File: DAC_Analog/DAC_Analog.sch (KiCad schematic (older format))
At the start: 17 parts, among them J1 SPDIF_RX_1, J2 SPDIF_RX_2, J3 SPDIF_RX_3, J4 SPDIF_RX_4, J5 I2C_IN, J6 OutR, J7 OutL, J8 Alim_DAC, J9 Alim_SRC, U1 ISO154x

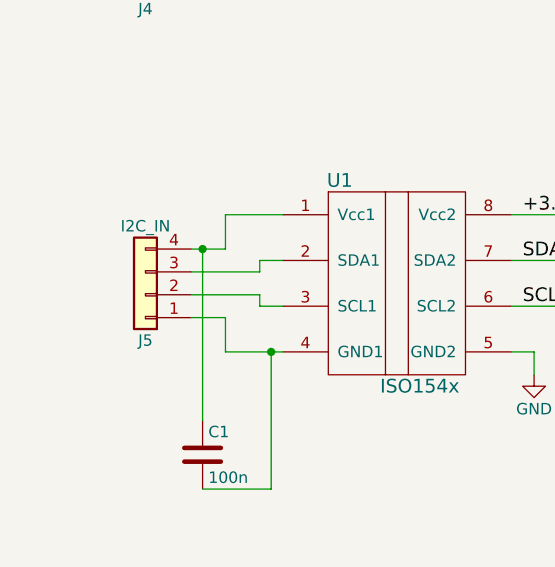
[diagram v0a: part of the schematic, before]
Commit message: Place cmp DAC_Analog
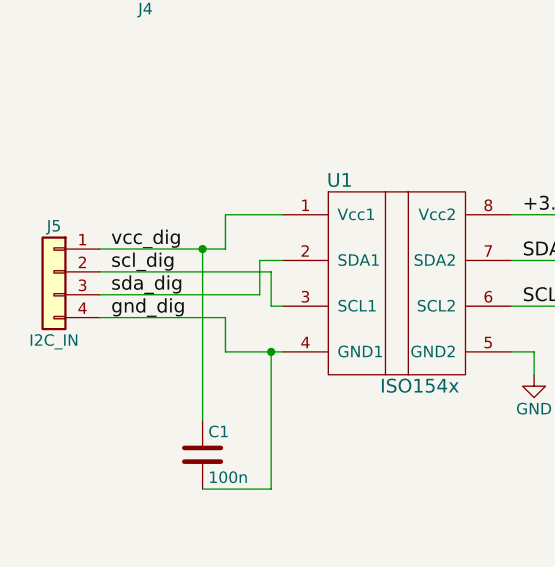
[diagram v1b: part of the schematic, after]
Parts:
- C3, C4, C5, C6, C7: footprint Capacitors_THT:CP_Radial_Tantal_D8.0mm_P2.50mm -> Capacitors_Tantalum_SMD:CP_Tantalum_Case-C_EIA-6032-28_Hand
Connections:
- net labels added: gnd_dig, scl_dig, sda_dig, vcc_dig
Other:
- moved on the sheet: J5
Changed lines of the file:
@@
 L Conn_01x04 J5
 U 1 1 59C97424
-P 1300 3800
-F 0 "J5" H 1300 4000 50  0000 C CNN
-F 1 "I2C_IN" H 1300 3500 50  0000 C CNN
-F 2 "Pin_Headers:Pin_Header_Straight_1x04_Pitch2.54mm" H 1300 3800 50  0001 C CNN
-F 3 "" H 1300 3800 50  0001 C CNN
-	1    1300 3800
-	-1   0    0    1
+P 900 3700
+F 0 "J5" H 900 3900 50  0000 C CNN
+F 1 "I2C_IN" H 900 3400 50  0000 C CNN
+F 2 "Pin_Headers:Pin_Header_Straight_1x04_Pitch2.54mm" H 900 3700 50  0001 C CNN
+F 3 "" H 900 3700 50  0001 C CNN
+	1    900  3700
+	-1   0    0    -1
 $EndComp
 $Comp
@@
 	2900 3450 3700 3450
 Wire Wire Line
-	1500 3600 1650 3600
+	1100 3600 1650 3600
 Wire Wire Line
 	1650 3600 1650 3450
@@
 	1650 3450 1900 3450
 Wire Wire Line
-	1500 3700 1800 3700
-Wire Wire Line
-	1800 3700 1800 3650
-Wire Wire Line
-	1800 3650 1900 3650
-Wire Wire Line
-	1500 3800 1800 3800
-Wire Wire Line
-	1800 3800 1800 3850
-Wire Wire Line
-	1800 3850 1900 3850
-Wire Wire Line
-	1500 3900 1650 3900
+	1100 3800 1800 3800
+Wire Wire Line
+	1100 3900 1650 3900
 Wire Wire Line
 	1650 3900 1650 4050
@@
 F 0 "C4" H 4475 5550 50  0000 L CNN
 F 1 "100u" H 4475 5350 50  0000 L CNN
-F 2 "Capacitors_THT:CP_Radial_Tantal_D8.0mm_P2.50mm" H 4488 5300 50  0001 C CNN
+F 2 "Capacitors_Tantalum_SMD:CP_Tantalum_Case-C_EIA-6032-28_Hand" H 4488 5300 50  0001 C CNN
 F 3 "" H 4450 5450 50  0001 C CNN
 	1    4450 5450
@@
 F 0 "C6" H 5225 5550 50  0000 L CNN
 F 1 "100u" H 5225 5350 50  0000 L CNN
-F 2 "Capacitors_THT:CP_Radial_Tantal_D8.0mm_P2.50mm" H 5238 5300 50  0001 C CNN
+F 2 "Capacitors_Tantalum_SMD:CP_Tantalum_Case-C_EIA-6032-28_Hand" H 5238 5300 50  0001 C CNN
 F 3 "" H 5200 5450 50  0001 C CNN
 	1    5200 5450
@@
 F 0 "C7" H 5975 5550 50  0000 L CNN
 F 1 "100u" H 5975 5350 50  0000 L CNN
-F 2 "Capacitors_THT:CP_Radial_Tantal_D8.0mm_P2.50mm" H 5988 5300 50  0001 C CNN
+F 2 "Capacitors_Tantalum_SMD:CP_Tantalum_Case-C_EIA-6032-28_Hand" H 5988 5300 50  0001 C CNN
 F 3 "" H 5950 5450 50  0001 C CNN
 	1    5950 5450
@@
 F 0 "C5" H 5175 6400 50  0000 L CNN
 F 1 "100u" H 5175 6200 50  0000 L CNN
-F 2 "Capacitors_THT:CP_Radial_Tantal_D8.0mm_P2.50mm" H 5188 6150 50  0001 C CNN
+F 2 "Capacitors_Tantalum_SMD:CP_Tantalum_Case-C_EIA-6032-28_Hand" H 5188 6150 50  0001 C CNN
 F 3 "" H 5150 6300 50  0001 C CNN
 	1    5150 6300
@@
 F 0 "C3" H 4425 6400 50  0000 L CNN
 F 1 "100u" H 4425 6200 50  0000 L CNN
-F 2 "Capacitors_THT:CP_Radial_Tantal_D8.0mm_P2.50mm" H 4438 6150 50  0001 C CNN
+F 2 "Capacitors_Tantalum_SMD:CP_Tantalum_Case-C_EIA-6032-28_Hand" H 4438 6150 50  0001 C CNN
 F 3 "" H 4400 6300 50  0001 C CNN
 	1    4400 6300
@@
 Wire Wire Line
 	7750 3850 8250 3850
+Text Label 1150 3900 0    60   ~ 0
+gnd_dig
+Text Label 1150 3700 0    60   ~ 0
+scl_dig
+Text Label 1150 3800 0    60   ~ 0
+sda_dig
+Text Label 1150 3600 0    60   ~ 0
+vcc_dig
+Wire Wire Line
+	1100 3700 1850 3700
+Wire Wire Line
+	1850 3700 1850 3850
+Wire Wire Line
+	1850 3850 1900 3850
+Wire Wire Line
+	1800 3800 1800 3650
+Wire Wire Line
+	1800 3650 1900 3650
 $EndSCHEMATC

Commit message: Update layout
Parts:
- added D1, D2, D3, D4, D5: LED, Yame_library:SM0603-LED-MR, symbol LED
- added R31, R32, R33, R34, R35: R, Yame_library:SM0603-MR, symbol R
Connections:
- wire segments 91 -> 106
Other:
- moved on the sheet: C3, C4, C5, C7

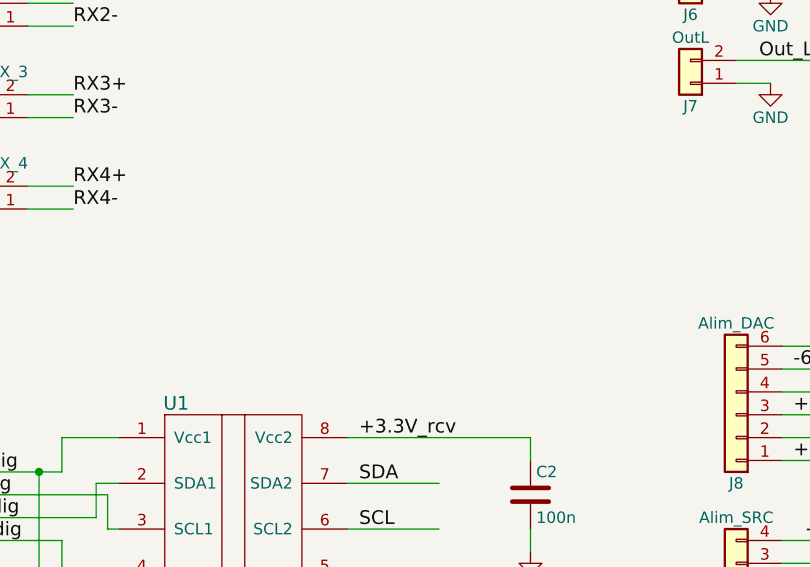
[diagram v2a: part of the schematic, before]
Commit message: DAC_Analog : place all cmp
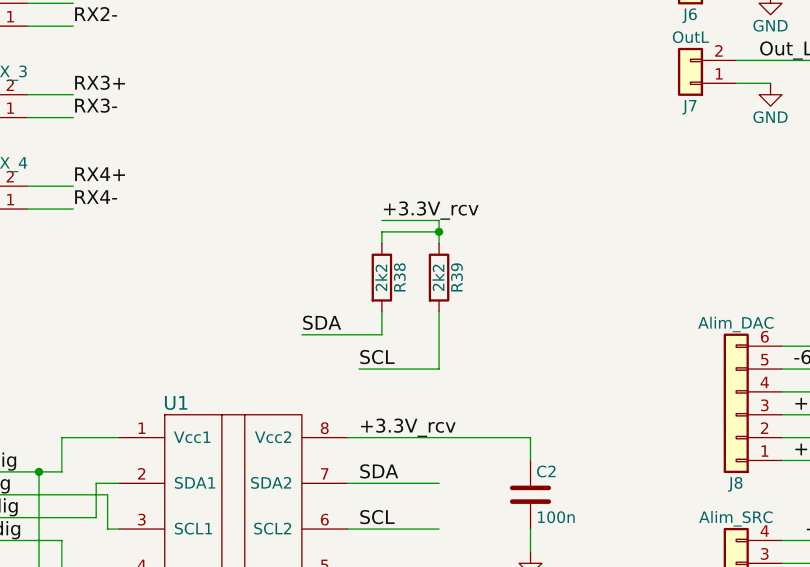
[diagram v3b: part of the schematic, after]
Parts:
- added R38, R39: 2k2, Yame_library:SM0603-MR, symbol R
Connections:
- wire segments 106 -> 114
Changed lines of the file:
@@
 	1650 4050 1900 4050
 $Comp
-L GND #PWR01
+L GND #PWR1
 U 1 1 59CB983A
 P 3000 4150
-F 0 "#PWR01" H 3000 3900 50  0001 C CNN
+F 0 "#PWR1" H 3000 3900 50  0001 C CNN
 F 1 "GND" H 3000 4000 50  0000 C CNN
 F 2 "" H 3000 4150 50  0001 C CNN
@@
 	7850 2250 8250 2250
 $Comp
-L GND #PWR02
+L GND #PWR17
 U 1 1 59CBC1FC
 P 7750 4100
-F 0 "#PWR02" H 7750 3850 50  0001 C CNN
+F 0 "#PWR17" H 7750 3850 50  0001 C CNN
 F 1 "GND" H 7750 3950 50  0000 C CNN
 F 2 "" H 7750 4100 50  0001 C CNN
@@
 	7750 4000 7750 4100
 $Comp
-L GND #PWR03
+L GND #PWR16
 U 1 1 59CBC549
 P 7500 1450
-F 0 "#PWR03" H 7500 1200 50  0001 C CNN
+F 0 "#PWR16" H 7500 1200 50  0001 C CNN
 F 1 "GND" H 7500 1300 50  0000 C CNN
 F 2 "" H 7500 1450 50  0001 C CNN
@@
 	4600 1800 5000 1800
 $Comp
-L GND #PWR04
+L GND #PWR7
 U 1 1 59CBD970
 P 4750 1500
-F 0 "#PWR04" H 4750 1250 50  0001 C CNN
+F 0 "#PWR7" H 4750 1250 50  0001 C CNN
 F 1 "GND" H 4750 1350 50  0000 C CNN
 F 2 "" H 4750 1500 50  0001 C CNN
@@
 $EndComp
 $Comp
-L GND #PWR05
+L GND #PWR8
 U 1 1 59CBD9E8
 P 4750 1900
-F 0 "#PWR05" H 4750 1650 50  0001 C CNN
+F 0 "#PWR8" H 4750 1650 50  0001 C CNN
 F 1 "GND" H 4750 1750 50  0000 C CNN
 F 2 "" H 4750 1900 50  0001 C CNN
@@
 	3700 3450 3700 3550
 $Comp
-L GND #PWR06
+L GND #PWR2
 U 1 1 59CC829B
 P 3700 3950
-F 0 "#PWR06" H 3700 3700 50  0001 C CNN
+F 0 "#PWR2" H 3700 3700 50  0001 C CNN
 F 1 "GND" H 3700 3800 50  0000 C CNN
 F 2 "" H 3700 3950 50  0001 C CNN
@@
 $EndComp
 $Comp
-L GND #PWR07
+L GND #PWR12
 U 1 1 59CC3026
 P 5450 4300
-F 0 "#PWR07" H 5450 4050 50  0001 C CNN
+F 0 "#PWR12" H 5450 4050 50  0001 C CNN
 F 1 "GND" H 5450 4150 50  0000 C CNN
 F 2 "" H 5450 4300 50  0001 C CNN
@@
 $EndComp
 $Comp
-L GND #PWR08
+L GND #PWR4
 U 1 1 59CCA544
 P 4350 5700
-F 0 "#PWR08" H 4350 5450 50  0001 C CNN
+F 0 "#PWR4" H 4350 5450 50  0001 C CNN
 F 1 "GND" H 4350 5550 50  0000 C CNN
 F 2 "" H 4350 5700 50  0001 C CNN
@@
 $EndComp
 $Comp
-L GND #PWR09
+L GND #PWR10
 U 1 1 59CCA62A
 P 5200 5700
-F 0 "#PWR09" H 5200 5450 50  0001 C CNN
+F 0 "#PWR10" H 5200 5450 50  0001 C CNN
 F 1 "GND" H 5200 5550 50  0000 C CNN
 F 2 "" H 5200 5700 50  0001 C CNN
@@
 $EndComp
 $Comp
-L GND #PWR010
+L GND #PWR15
 U 1 1 59CCA710
 P 6050 5700
-F 0 "#PWR010" H 6050 5450 50  0001 C CNN
+F 0 "#PWR15" H 6050 5450 50  0001 C CNN
 F 1 "GND" H 6050 5550 50  0000 C CNN
 F 2 "" H 6050 5700 50  0001 C CNN
@@
 $EndComp
 $Comp
-L GND #PWR011
+L GND #PWR14
 U 1 1 59CCA7F6
 P 5700 6950
-F 0 "#PWR011" H 5700 6700 50  0001 C CNN
+F 0 "#PWR14" H 5700 6700 50  0001 C CNN
 F 1 "GND" H 5700 6800 50  0000 C CNN
 F 2 "" H 5700 6950 50  0001 C CNN
@@
 $EndComp
 $Comp
-L GND #PWR012
+L GND #PWR9
 U 1 1 59CCA8DC
 P 4950 6950
-F 0 "#PWR012" H 4950 6700 50  0001 C CNN
+F 0 "#PWR9" H 4950 6700 50  0001 C CNN
 F 1 "GND" H 4950 6800 50  0000 C CNN
 F 2 "" H 4950 6950 50  0001 C CNN
@@
 $EndComp
 $Comp
-L GND #PWR013
+L GND #PWR13
 U 1 1 59EF6504
 P 5550 6000
-F 0 "#PWR013" H 5550 5750 50  0001 C CNN
+F 0 "#PWR13" H 5550 5750 50  0001 C CNN
 F 1 "GND" H 5550 5850 50  0000 C CNN
 F 2 "" H 5550 6000 50  0001 C CNN
@@
 $EndComp
 $Comp
-L GND #PWR014
+L GND #PWR3
 U 1 1 59EF74CB
 P 3850 6000
-F 0 "#PWR014" H 3850 5750 50  0001 C CNN
+F 0 "#PWR3" H 3850 5750 50  0001 C CNN
 F 1 "GND" H 3850 5850 50  0000 C CNN
 F 2 "" H 3850 6000 50  0001 C CNN
@@
 $EndComp
 $Comp
-L GND #PWR015
+L GND #PWR6
 U 1 1 59EF75DC
 P 4700 6000
-F 0 "#PWR015" H 4700 5750 50  0001 C CNN
+F 0 "#PWR6" H 4700 5750 50  0001 C CNN
 F 1 "GND" H 4700 5850 50  0000 C CNN
 F 2 "" H 4700 6000 50  0001 C CNN
@@
 $EndComp
 $Comp
-L GND #PWR016
+L GND #PWR5
 U 1 1 59EF7B17
 P 4500 7250
-F 0 "#PWR016" H 4500 7000 50  0001 C CNN
+F 0 "#PWR5" H 4500 7000 50  0001 C CNN
 F 1 "GND" H 4500 7100 50  0000 C CNN
 F 2 "" H 4500 7250 50  0001 C CNN
@@
 $EndComp
 $Comp
-L GND #PWR017
+L GND #PWR11
 U 1 1 59EF7C3C
 P 5250 7250
-F 0 "#PWR017" H 5250 7000 50  0001 C CNN
+F 0 "#PWR11" H 5250 7000 50  0001 C CNN
 F 1 "GND" H 5250 7100 50  0000 C CNN
 F 2 "" H 5250 7250 50  0001 C CNN
@@
 Wire Wire Line
 	5250 6550 5250 6450
+$Comp
+L R R38
+U 1 1 59EFD621
+P 3050 2750
+F 0 "R38" V 3130 2750 50  0000 C CNN
+F 1 "2k2" V 3050 2750 50  0000 C CNN
+F 2 "Yame_library:SM0603-MR" V 2980 2750 50  0001 C CNN
+F 3 "" H 3050 2750 50  0001 C CNN
+	1    3050 2750
+	1    0    0    -1
+$EndComp
+$Comp
+L R R39
+U 1 1 59EFDBA2
+P 3300 2750
+F 0 "R39" V 3380 2750 50  0000 C CNN
+F 1 "2k2" V 3300 2750 50  0000 C CNN
+F 2 "Yame_library:SM0603-MR" V 3230 2750 50  0001 C CNN
+F 3 "" H 3300 2750 50  0001 C CNN
+	1    3300 2750
+	1    0    0    -1
+$EndComp
+Text Label 3050 2500 0    60   ~ 0
++3.3V_rcv
+Wire Wire Line
+	3050 2500 3300 2500
+Wire Wire Line
+	3300 2500 3300 2600
+Wire Wire Line
+	3050 2600 3050 2550
+Wire Wire Line
+	3050 2550 3300 2550
+Connection ~ 3300 2550
+Text Label 2950 3150 0    60   ~ 0
+SCL
+Text Label 2700 3000 0    60   ~ 0
+SDA
+Wire Wire Line
+	2950 3150 3300 3150
+Wire Wire Line
+	3050 3000 2700 3000
+Wire Wire Line
+	3050 3000 3050 2900
+Wire Wire Line
+	3300 3150 3300 2900
 $EndSCHEMATC

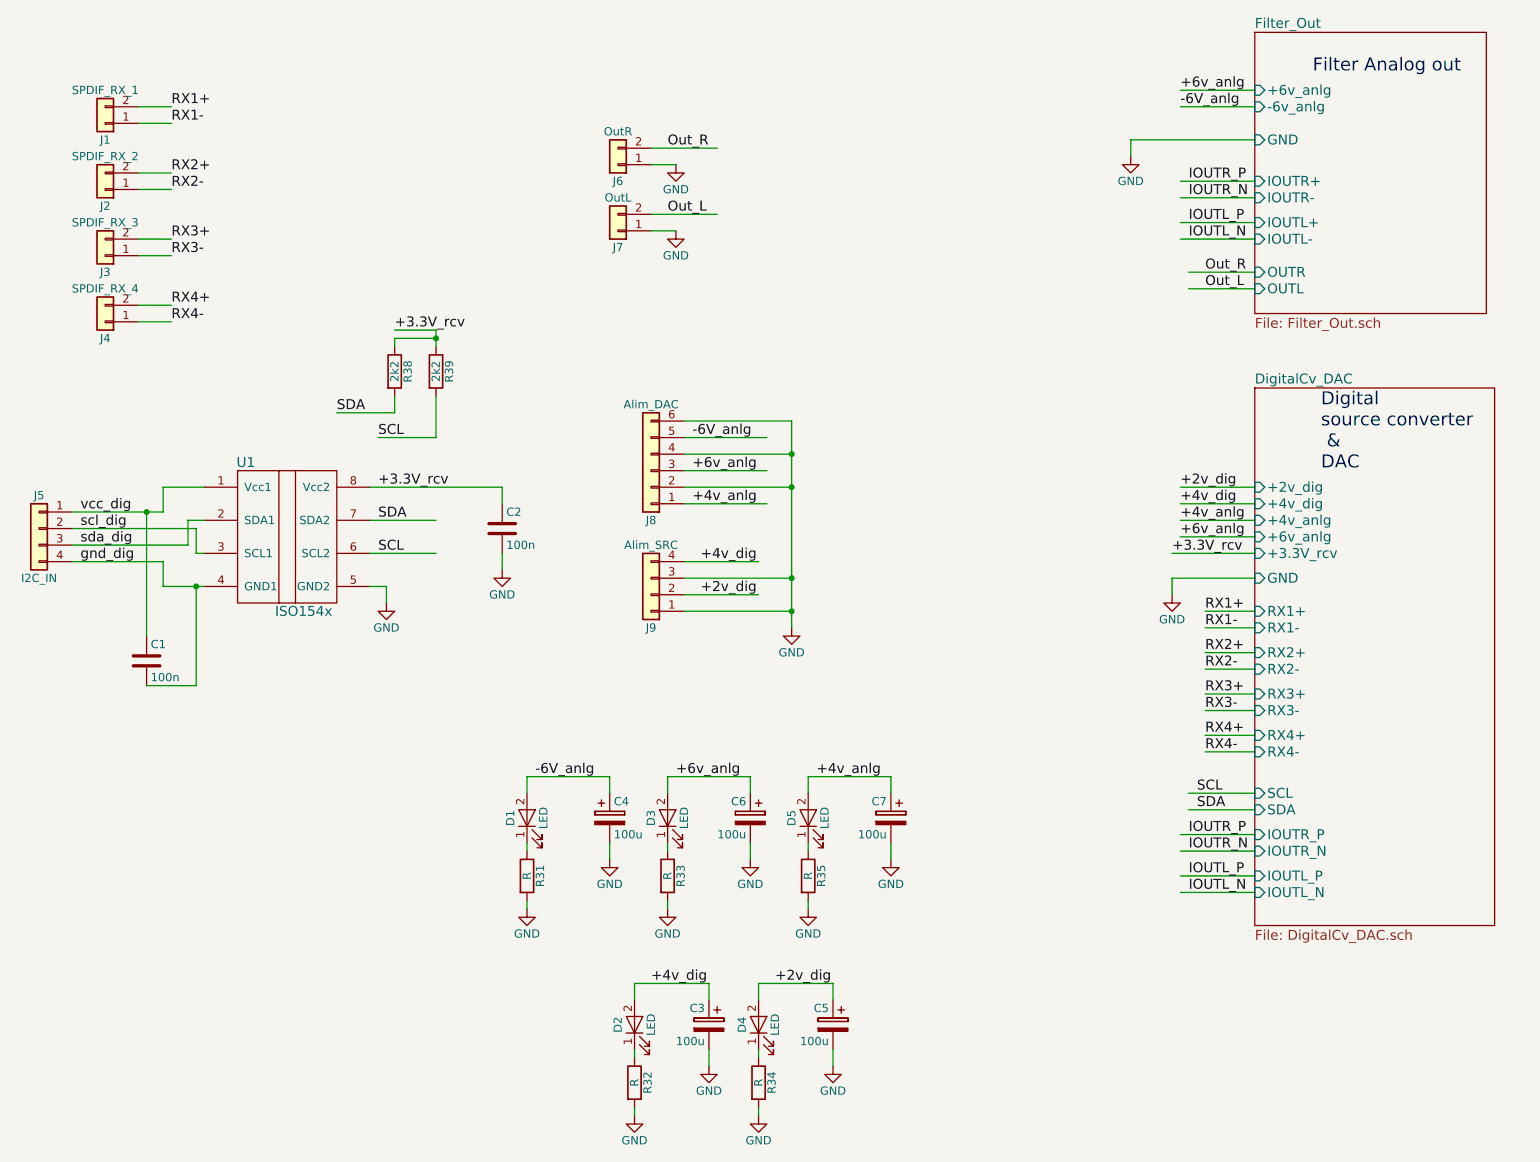
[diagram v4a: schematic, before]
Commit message: Send Gerber DAC_Analog and DAC_Digital
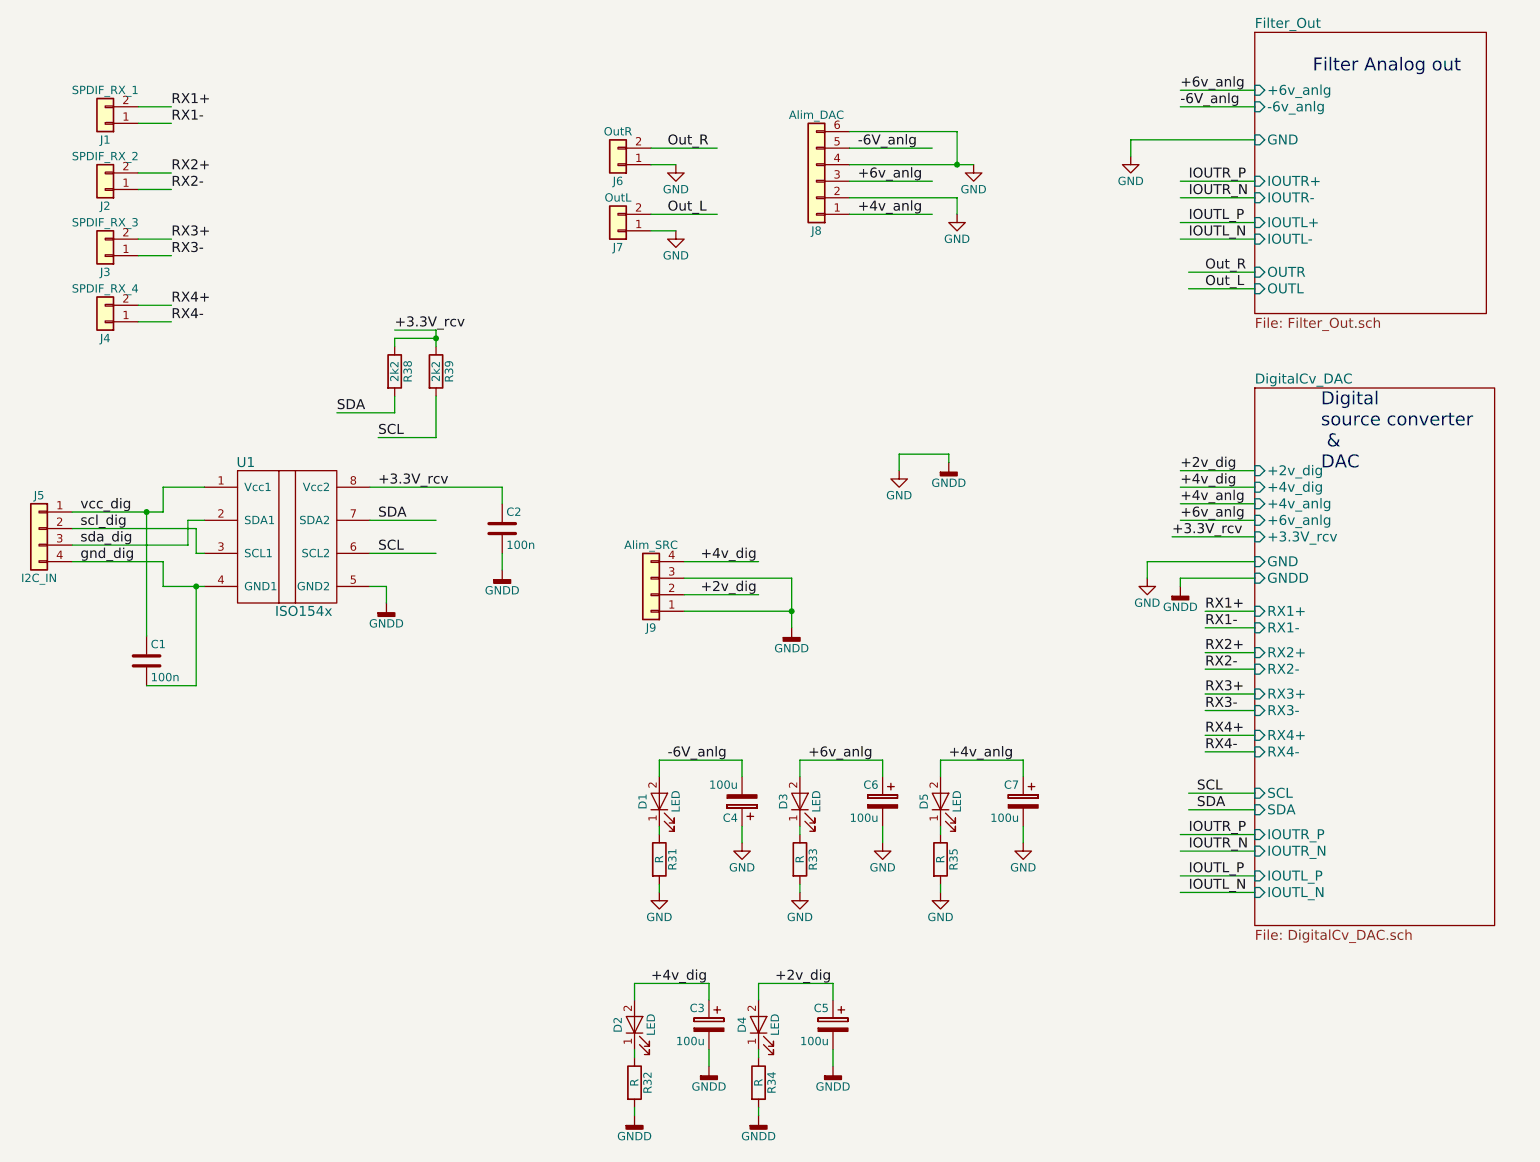
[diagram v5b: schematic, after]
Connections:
- net labels added: GNDD
- wire segments 114 -> 121
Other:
- moved on the sheet: C4, C6, C7, D1, D3, D5, J8, R31, R33, R35
